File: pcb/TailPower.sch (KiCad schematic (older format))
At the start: 9 parts

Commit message: Adds more to the schematic
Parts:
- C? (x4): footprint (none) -> Capacitor_SMD:C_0805_2012Metric
- J?, SW?: footprint (none) -> Connector_PinHeader_2.54mm:PinHeader_1x02_P2.54mm_Vertical
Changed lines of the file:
@@
 $Descr A4 11693 8268
 encoding utf-8
-Sheet 3 3
+Sheet 3 14
 Title ""
 Date ""
@@
 F 0 "C?" H 3365 2496 50  0000 L CNN
 F 1 "10μF" H 3365 2405 50  0000 L CNN
-F 2 "" H 3288 2300 50  0001 C CNN
+F 2 "Capacitor_SMD:C_0805_2012Metric" H 3288 2300 50  0001 C CNN
 F 3 "~" H 3250 2450 50  0001 C CNN
 	1    3250 2450
@@
 F 0 "C?" H 4615 2496 50  0000 L CNN
 F 1 "22μF" H 4615 2405 50  0000 L CNN
-F 2 "" H 4538 2300 50  0001 C CNN
+F 2 "Capacitor_SMD:C_0805_2012Metric" H 4538 2300 50  0001 C CNN
 F 3 "~" H 4500 2450 50  0001 C CNN
 	1    4500 2450
@@
 F 0 "C?" H 5165 2496 50  0000 L CNN
 F 1 "1μF" H 5165 2405 50  0000 L CNN
-F 2 "" H 5088 2300 50  0001 C CNN
+F 2 "Capacitor_SMD:C_0805_2012Metric" H 5088 2300 50  0001 C CNN
 F 3 "~" H 5050 2450 50  0001 C CNN
 	1    5050 2450
@@
 F 0 "C?" H 6065 2496 50  0000 L CNN
 F 1 "1μF" H 6065 2405 50  0000 L CNN
-F 2 "" H 5988 2300 50  0001 C CNN
+F 2 "Capacitor_SMD:C_0805_2012Metric" H 5988 2300 50  0001 C CNN
 F 3 "~" H 5950 2450 50  0001 C CNN
 	1    5950 2450
@@
 F 0 "J?" H 1907 1817 50  0000 C CNN
 F 1 "Barrel_Jack_Switch_Pin3Ring" H 1907 1726 50  0000 C CNN
-F 2 "" H 1900 1460 50  0001 C CNN
+F 2 "Connector_PinHeader_2.54mm:PinHeader_1x02_P2.54mm_Vertical" H 1900 1460 50  0001 C CNN
 F 3 "~" H 1900 1460 50  0001 C CNN
 	1    1850 1500
@@
 F 0 "SW?" H 2850 2335 50  0000 C CNN
 F 1 "SW_SPST" H 2850 2244 50  0000 C CNN
-F 2 "" H 2850 2100 50  0001 C CNN
+F 2 "Connector_PinHeader_2.54mm:PinHeader_1x02_P2.54mm_Vertical" H 2850 2100 50  0001 C CNN
 F 3 "~" H 2850 2100 50  0001 C CNN
 	1    2850 2100

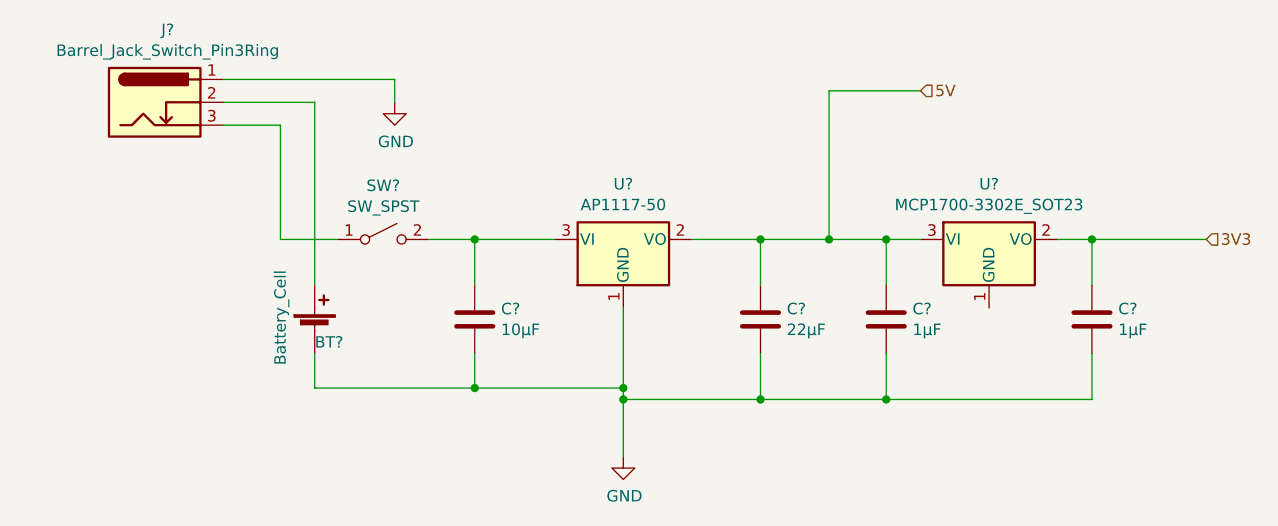
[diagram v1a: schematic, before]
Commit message: Completes first cut of the schematic
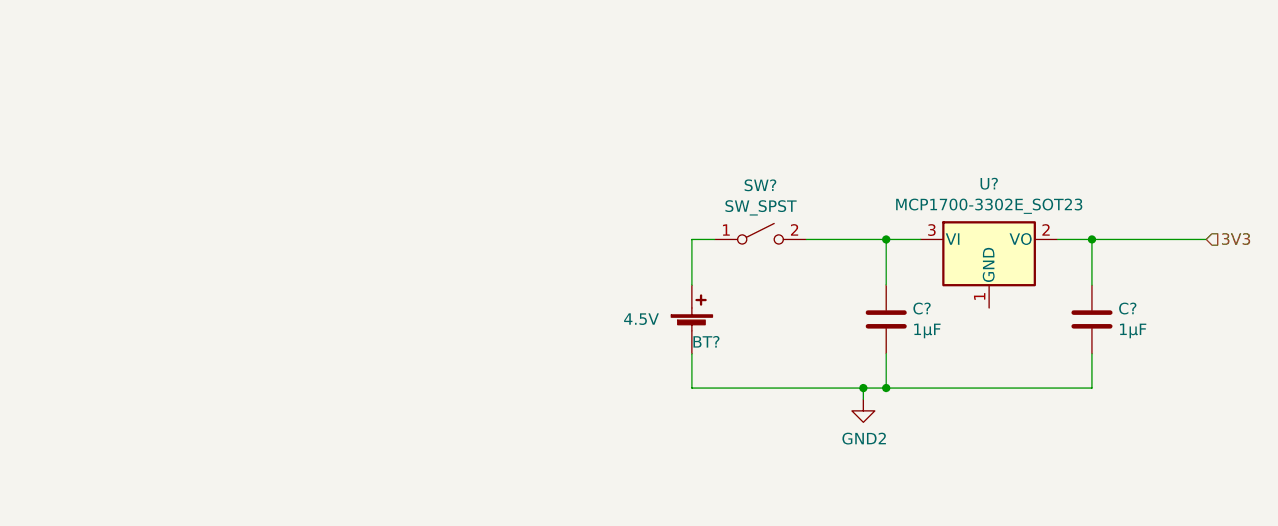
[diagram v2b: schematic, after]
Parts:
- removed C?: 10μF, Capacitor_SMD:C_0805_2012Metric, symbol Device:C
- removed C?: 22μF, Capacitor_SMD:C_0805_2012Metric, symbol Device:C
- removed J?: Barrel_Jack_Switch_Pin3Ring, Connector_PinHeader_2.54mm:PinHeader_1x02_P2.54mm_Vertical, symbol Connector:Barrel_Jack_Switch_Pin3Ring
- removed U?: AP1117-50, Package_TO_SOT_SMD:SOT-223-3_TabPin2, symbol Regulator_Linear:AP1117-50
- BT?: value Battery_Cell -> 4.5V
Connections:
- net 5V is gone; now on an unnamed net: C?.1, U?.3 (VI)
- net at BT?.1 (+): now also SW?.1 (A)
- net GND renamed GND2
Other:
- moved on the sheet: BT?, SW?
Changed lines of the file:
@@
-$EndComp
-$Comp
-L Regulator_Linear:AP1117-50 U?
-U 1 1 61B54B58
-P 3900 2100
-AR Path="/61B54B58" Ref="U?"  Part="1"
-AR Path="/61AE2AA5/61B54B58" Ref="U?"  Part="1"
-AR Path="/61B47BFA/61B54B58" Ref="U?"  Part="1"
-F 0 "U?" H 3900 2342 50  0000 C CNN
-F 1 "AP1117-50" H 3900 2251 50  0000 C CNN
-F 2 "Package_TO_SOT_SMD:SOT-223-3_TabPin2" H 3900 2300 50  0001 C CNN
-F 3 "http://www.diodes.com/datasheets/AP1117.pdf" H 4000 1850 50  0001 C CNN
-	1    3900 2100
-	1    0    0    -1
 $EndComp
 $Comp
 L Device:Battery_Cell BT?
 U 1 1 61B54B5E
-P 2550 2500
+P 4200 2500
 AR Path="/61B54B5E" Ref="BT?"  Part="1"
 AR Path="/61AE2AA5/61B54B5E" Ref="BT?"  Part="1"
 AR Path="/61B47BFA/61B54B5E" Ref="BT?"  Part="1"
-F 0 "BT?" H 2550 2450 50  0000 L CNN
-F 1 "Battery_Cell" V 2400 2350 50  0000 L CNN
-F 2 "CoaxTester:BATT_CONN" V 2550 2560 50  0001 C CNN
-F 3 "~" V 2550 2560 50  0001 C CNN
-	1    2550 2500
+F 0 "BT?" H 4200 2450 50  0000 L CNN
+F 1 "4.5V" H 3900 2550 50  0000 L CNN
+F 2 "CoaxTester:BATT_CONN" V 4200 2560 50  0001 C CNN
+F 3 "~" V 4200 2560 50  0001 C CNN
+	1    4200 2500
 	1    0    0    -1
 $EndComp
-$Comp
-L Device:C C?
-U 1 1 61B54B64
-P 3250 2450
-F 0 "C?" H 3365 2496 50  0000 L CNN
-F 1 "10μF" H 3365 2405 50  0000 L CNN
-F 2 "Capacitor_SMD:C_0805_2012Metric" H 3288 2300 50  0001 C CNN
-F 3 "~" H 3250 2450 50  0001 C CNN
-	1    3250 2450
-	1    0    0    -1
-$EndComp
-$Comp
-L Device:C C?
-U 1 1 61B54B6A
-P 4500 2450
-F 0 "C?" H 4615 2496 50  0000 L CNN
-F 1 "22μF" H 4615 2405 50  0000 L CNN
-F 2 "Capacitor_SMD:C_0805_2012Metric" H 4538 2300 50  0001 C CNN
-F 3 "~" H 4500 2450 50  0001 C CNN
-	1    4500 2450
-	1    0    0    -1
-$EndComp
-$Comp
-L power:GND #PWR?
-U 1 1 61B54B70
-P 3900 3050
-F 0 "#PWR?" H 3900 2800 50  0001 C CNN
-F 1 "GND" H 3905 2877 50  0000 C CNN
-F 2 "" H 3900 3050 50  0001 C CNN
-F 3 "" H 3900 3050 50  0001 C CNN
-	1    3900 3050
-	1    0    0    -1
-$EndComp
-Wire Wire Line
-	3250 2300 3250 2100
-Connection ~ 3250 2100
-Wire Wire Line
-	3250 2600 3250 2750
-Wire Wire Line
-	3250 2750 3900 2750
-Connection ~ 3900 2750
-Wire Wire Line
-	3900 2750 3900 2800
-Wire Wire Line
-	2550 2750 3250 2750
-Connection ~ 3250 2750
-Wire Wire Line
-	3900 2400 3900 2750
-Wire Wire Line
-	4500 2600 4500 2800
-Wire Wire Line
-	4500 2800 3900 2800
-Connection ~ 3900 2800
-Wire Wire Line
-	3900 2800 3900 3050
-Wire Wire Line
-	4500 2300 4500 2100
-Wire Wire Line
-	4500 2100 4200 2100
-Wire Wire Line
-	4500 2100 4800 2100
-Connection ~ 4500 2100
 $Comp
 L Device:C C?
@@
 $EndComp
 Wire Wire Line
-	4800 2100 4800 1450
-Wire Wire Line
-	4800 1450 5200 1450
-Wire Wire Line
-	4800 2100 5050 2100
-Connection ~ 4800 2100
-Wire Wire Line
 	5050 2100 5050 2300
 Wire Wire Line
-	5950 2800 5950 2600
+	5950 2750 5950 2600
 Wire Wire Line
 	5950 2100 5800 2100
 Wire Wire Line
-	5050 2600 5050 2800
+	5050 2600 5050 2750
 Wire Wire Line
 	5950 2300 5950 2100
@@
 	5950 2100 6450 2100
 Connection ~ 5950 2100
-$Comp
-L Connector:Barrel_Jack_Switch_Pin3Ring J?
-U 1 1 61B54BA0
-P 1850 1500
-F 0 "J?" H 1907 1817 50  0000 C CNN
-F 1 "Barrel_Jack_Switch_Pin3Ring" H 1907 1726 50  0000 C CNN
-F 2 "Connector_PinHeader_2.54mm:PinHeader_1x02_P2.54mm_Vertical" H 1900 1460 50  0001 C CNN
-F 3 "~" H 1900 1460 50  0001 C CNN
-	1    1850 1500
-	1    0    0    -1
-$EndComp
 Wire Wire Line
-	2550 2300 2550 1500
+	4200 2750 4200 2600
 Wire Wire Line
-	3250 2100 3050 2100
-Wire Wire Line
-	3250 2100 3600 2100
-Wire Wire Line
-	2550 1500 2150 1500
-Wire Wire Line
-	2550 2750 2550 2600
-Wire Wire Line
-	4500 2800 5050 2800
-Connection ~ 4500 2800
-Connection ~ 5050 2800
-Wire Wire Line
-	5050 2800 5950 2800
-Wire Wire Line
-	2150 1400 2900 1400
-Wire Wire Line
-	2400 2100 2400 1600
-Wire Wire Line
-	2400 1600 2150 1600
-Wire Wire Line
-	2900 1400 2900 1500
-$Comp
-L power:GND #PWR?
-U 1 1 61B54BB3
-P 2900 1500
-F 0 "#PWR?" H 2900 1250 50  0001 C CNN
-F 1 "GND" H 2905 1327 50  0000 C CNN
-F 2 "" H 2900 1500 50  0001 C CNN
-F 3 "" H 2900 1500 50  0001 C CNN
-	1    2900 1500
-	1    0    0    -1
-$EndComp
-Text HLabel 5200 1450 2    50   Input ~ 0
-5V
+	5050 2750 5950 2750
 Text HLabel 6450 2100 2    50   Input ~ 0
 3V3
@@
 L Switch:SW_SPST SW?
 U 1 1 61B54BBB
-P 2850 2100
-F 0 "SW?" H 2850 2335 50  0000 C CNN
-F 1 "SW_SPST" H 2850 2244 50  0000 C CNN
-F 2 "Connector_PinHeader_2.54mm:PinHeader_1x02_P2.54mm_Vertical" H 2850 2100 50  0001 C CNN
-F 3 "~" H 2850 2100 50  0001 C CNN
-	1    2850 2100
+P 4500 2100
+F 0 "SW?" H 4500 2335 50  0000 C CNN
+F 1 "SW_SPST" H 4500 2244 50  0000 C CNN
+F 2 "Connector_PinHeader_2.54mm:PinHeader_1x02_P2.54mm_Vertical" H 4500 2100 50  0001 C CNN
+F 3 "~" H 4500 2100 50  0001 C CNN
+	1    4500 2100
 	1    0    0    -1
 $EndComp
 Wire Wire Line
-	2650 2100 2400 2100
+	4300 2100 4200 2100
+Wire Wire Line
+	4200 2300 4200 2100
+Wire Wire Line
+	4200 2750 4950 2750
+Connection ~ 5050 2750
+Wire Wire Line
+	4700 2100 5050 2100
+Wire Wire Line
+	4950 2800 4950 2750
+Connection ~ 4950 2750
+Wire Wire Line
+	4950 2750 5050 2750
+$Comp
+L power:GND2 #PWR?
+U 1 1 61BACFE8
+P 4950 2800
+F 0 "#PWR?" H 4950 2550 50  0001 C CNN
+F 1 "GND2" H 4955 2627 50  0000 C CNN
+F 2 "" H 4950 2800 50  0001 C CNN
+F 3 "" H 4950 2800 50  0001 C CNN
+	1    4950 2800
+	1    0    0    -1
+$EndComp
 $EndSCHEMATC
